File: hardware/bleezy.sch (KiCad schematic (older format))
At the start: 23 parts, among them P3 Raspberry_Pi_+_Conn

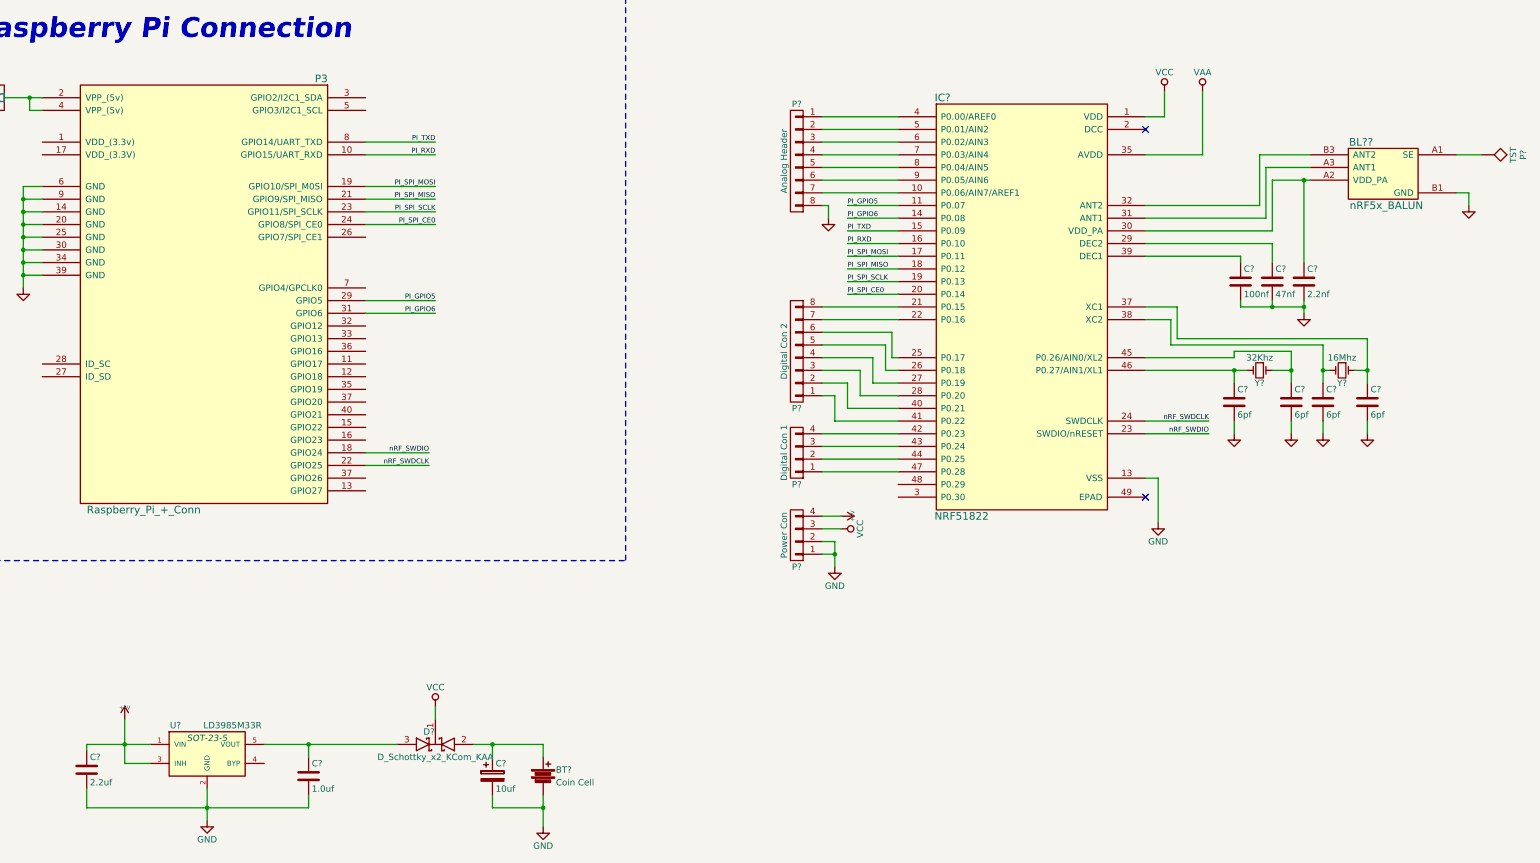
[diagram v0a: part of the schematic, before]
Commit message: added LED and vsense net
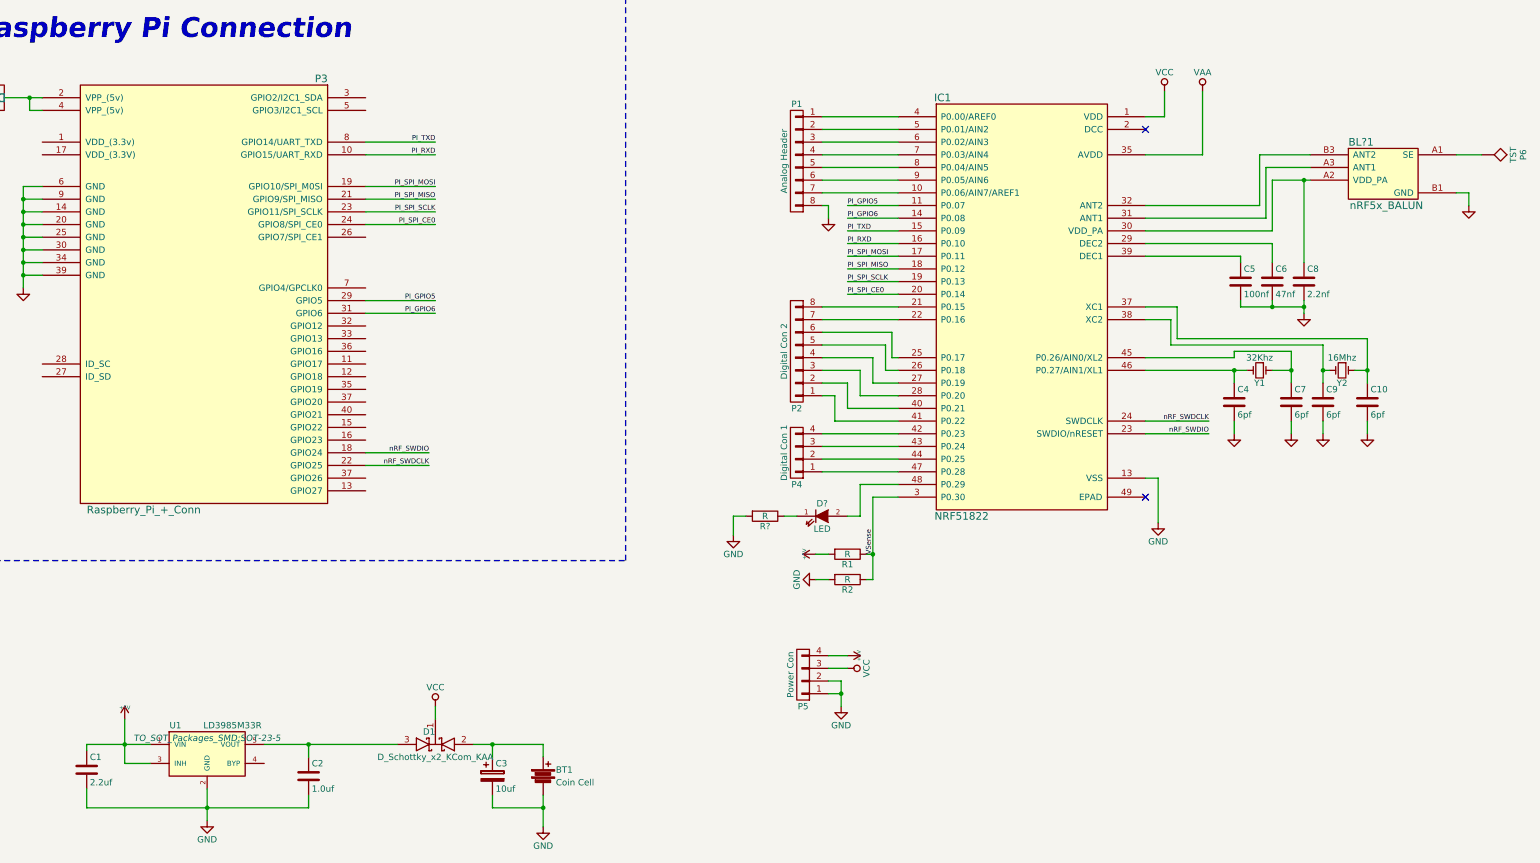
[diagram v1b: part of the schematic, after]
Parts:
- added D?: LED, symbol LED
- added R1, R2, R?: R, w_smd_resistors:r_0402, symbol R
- BL?1: renamed from BL??; footprint (none) -> openfet-footprint:BALUN_5BGA_ST
- BT1: renamed from BT?; footprint (none) -> openfet-footprint:keystone_3003
- C1, C10, C4, C5, C6, C7, C8, C9: renamed from C?; footprint (none) -> w_smd_cap:c_0402
- C2: renamed from C?; footprint (none) -> w_smd_cap:c_0603
- C3: renamed from C?; footprint (none) -> w_smd_cap:c_tant_B
- D1: renamed from D?; footprint (none) -> w_smd_trans:sot23
- IC1: renamed from IC?; footprint (none) -> w_smd_qfn:pvqfn-n48
- P1, P2: renamed from P?; footprint (none) -> w_pin_strip:pin_strip_8
- P4, P5: renamed from P?; footprint (none) -> w_pin_strip:pin_strip_4
- P6: renamed from P?; footprint (none) -> openfet-footprint:Ant_24ghz_small
- U1: renamed from U?; footprint SOT-23-5 -> TO_SOT_Packages_SMD:SOT-23-5
- Y1: renamed from Y?; footprint (none) -> w_crystal:crystal_tc-38_horiz
- Y2: renamed from Y?; footprint (none) -> w_crystal:crystal_fa128
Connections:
- net +5V: now also R1.2
- net GND: now also R2.2, R?.2
- net VSense: now reaches IC1.3 (P0.30)
- net VSense: now also R1.1, R2.1
- net at IC1.48 (P0.29): now also D?.2 (A)
- new net: D?.1 (K), R?.1
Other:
- moved on the sheet: P5

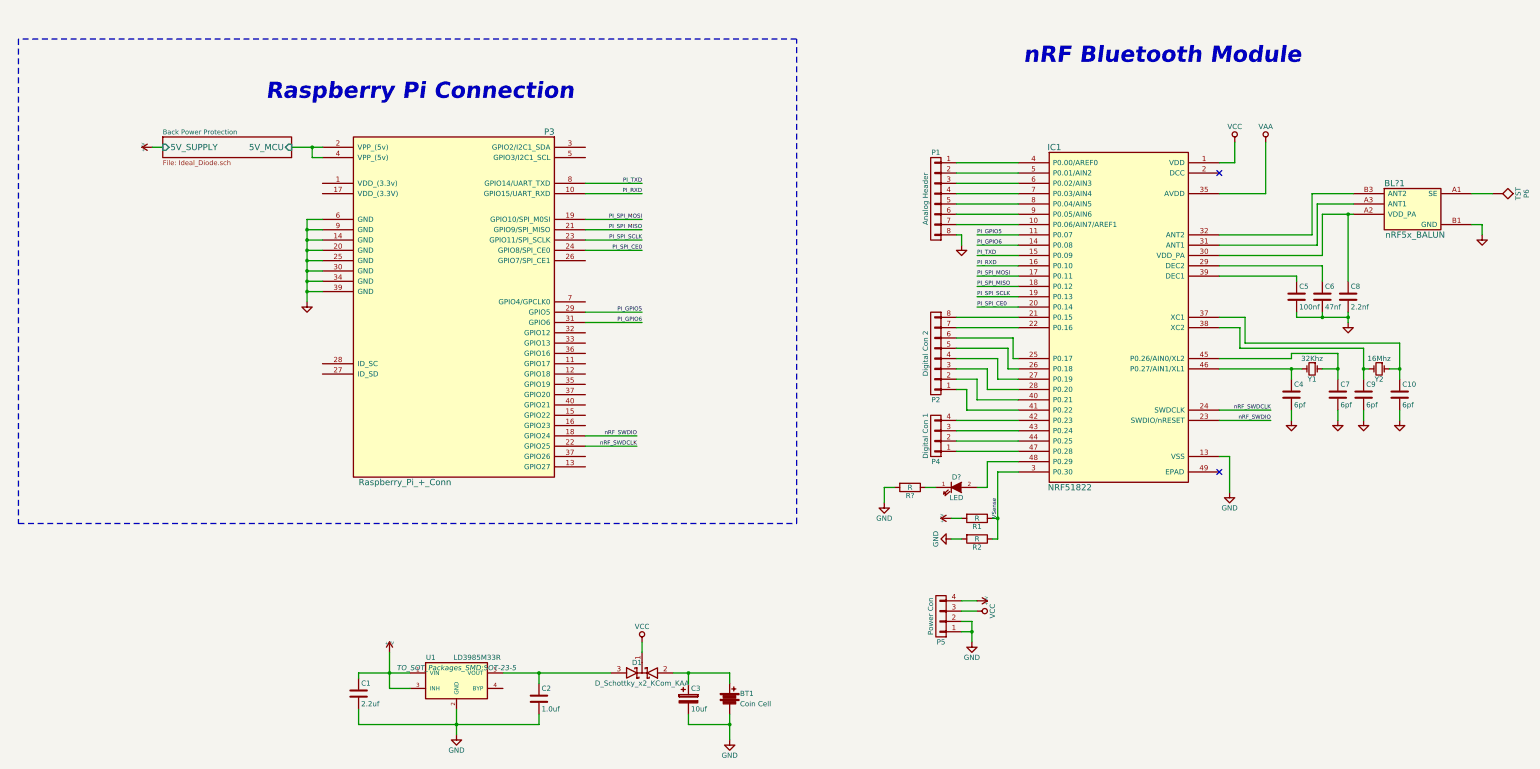
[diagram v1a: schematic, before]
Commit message: cleaned up schematic
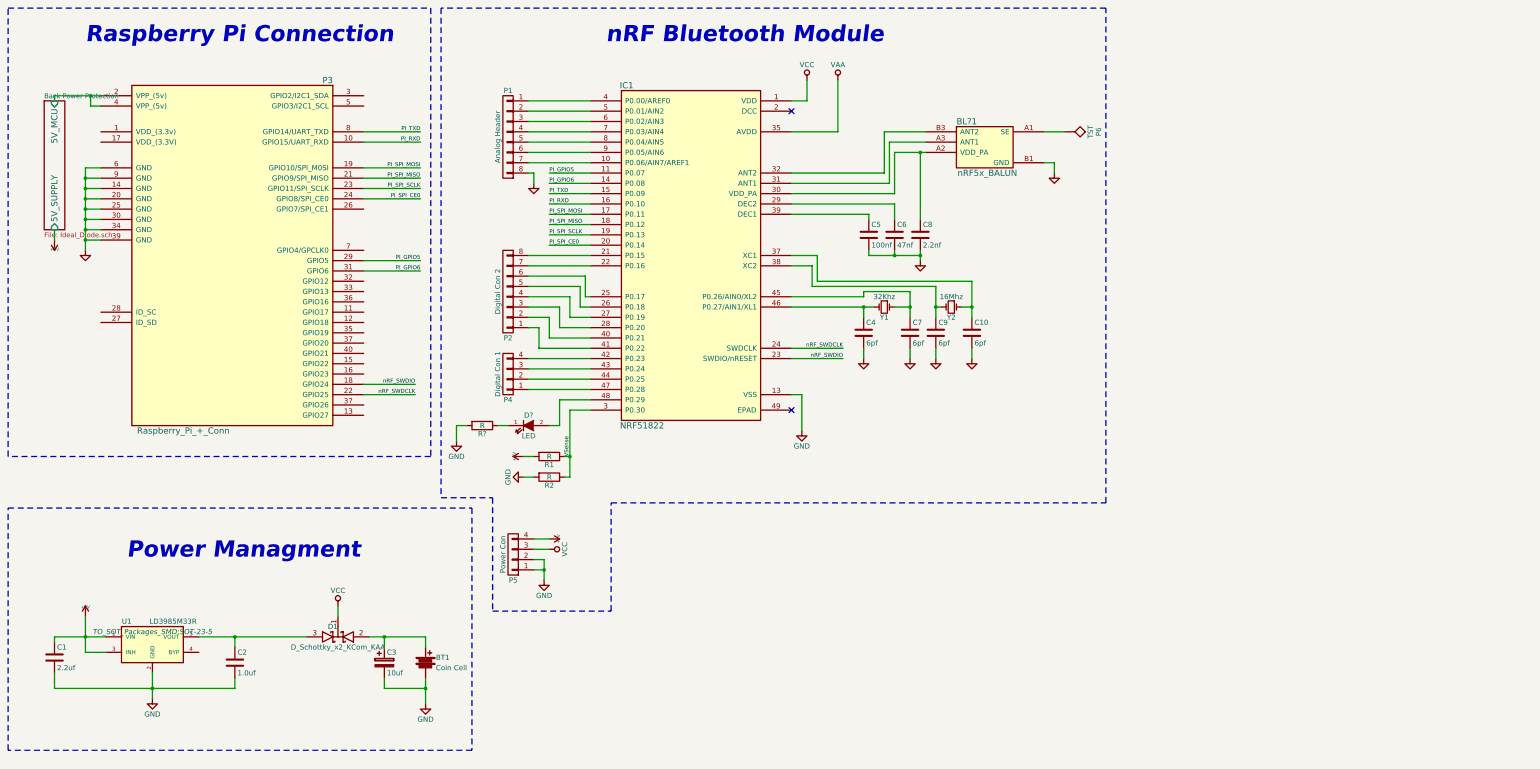
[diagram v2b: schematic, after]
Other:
- note added: "Power Managment"
- moved on the sheet: BL?1, BT1, C1, C10, C2, C3, C4, C5, C6, C7, C8, C9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

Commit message: removed monolithic balun
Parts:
- removed BL?1: nRF5x_BALUN, openfet-footprint:BALUN_5BGA_ST, symbol nRF5x_BALUN
- added C11: 2.2pf, w_smd_cap:c_0402, symbol C
- added C12: 1pf, w_smd_cap:c_0402, symbol C
- added C13: 1.5pf, w_smd_cap:c_0402, symbol C
- added JP1: JUMPER, w_smd_cap:c_0603, symbol JUMPER
- added L1: 4.7nH, w_smd_inductors:inductor_smd_0402, symbol INDUCTOR_SMALL
- added L2: 10nH, w_smd_inductors:inductor_smd_0402, symbol INDUCTOR_SMALL
- added L3: 3.3nH, w_smd_inductors:inductor_smd_0402, symbol INDUCTOR_SMALL
- D2: renamed from D?; footprint (none) -> w_smd_leds:Led_0603
- gave numbers to parts that had none: 1
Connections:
- net AVDD: now also JP1.2
- net GND: now also C12.1, C13.1
- net VCC: now also JP1.1
- net at C8.1, IC1.30 (VDD_PA): now also L2.1
- net at IC1.31 (ANT1): now also L1.1, L2.2
- net at IC1.32 (ANT2): now also C11.2, L1.2
- net at P6.1: now also C13.2, L3.1
- new net: C11.1, C12.2, L3.2
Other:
- moved on the sheet: P6

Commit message: redid basic layout, some routing
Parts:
- added C14, C15: 100nf, w_smd_cap:c_0402, symbol C
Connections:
- net GND: now also C14.2, C15.2
- net VCC: now also C14.1, C15.1
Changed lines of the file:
@@
 	0    -1   -1   0
 $EndComp
+$Comp
+L VCC #PWR027
+U 1 1 56861718
+P 10000 4450
+F 0 "#PWR027" H 10000 4300 50  0001 C CNN
+F 1 "VCC" H 10000 4600 50  0000 C CNN
+F 2 "" H 10000 4450 50  0000 C CNN
+F 3 "" H 10000 4450 50  0000 C CNN
+	1    10000 4450
+	1    0    0    -1
+$EndComp
+$Comp
+L C C14
+U 1 1 56861E04
+P 10000 4700
+F 0 "C14" H 10025 4800 50  0000 L CNN
+F 1 "100nf" H 10025 4600 50  0000 L CNN
+F 2 "w_smd_cap:c_0402" H 10038 4550 50  0001 C CNN
+F 3 "" H 10000 4700 50  0000 C CNN
+	1    10000 4700
+	1    0    0    -1
+$EndComp
+$Comp
+L GND #PWR028
+U 1 1 568620B4
+P 10000 4950
+F 0 "#PWR028" H 10000 4950 30  0001 C CNN
+F 1 "GND" H 10000 4880 30  0001 C CNN
+F 2 "" H 10000 4950 60  0000 C CNN
+F 3 "" H 10000 4950 60  0000 C CNN
+	1    10000 4950
+	1    0    0    -1
+$EndComp
+Wire Wire Line
+	10000 4550 10000 4450
+Wire Wire Line
+	10000 4850 10000 4950
+$Comp
+L C C15
+U 1 1 56862304
+P 10400 4700
+F 0 "C15" H 10425 4800 50  0000 L CNN
+F 1 "100nf" H 10425 4600 50  0000 L CNN
+F 2 "w_smd_cap:c_0402" H 10438 4550 50  0001 C CNN
+F 3 "" H 10400 4700 50  0000 C CNN
+	1    10400 4700
+	1    0    0    -1
+$EndComp
+Wire Wire Line
+	10000 4500 10400 4500
+Wire Wire Line
+	10400 4500 10400 4550
+Connection ~ 10000 4500
+Wire Wire Line
+	10000 4900 10400 4900
+Wire Wire Line
+	10400 4900 10400 4850
+Connection ~ 10000 4900
 $EndSCHEMATC

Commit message: finished routing
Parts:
- removed P4: Digital Con 1, w_pin_strip:pin_strip_4, symbol CONN_01X04
- D1: Mouser Part No. (none) -> 726-BAS7005E6327XT
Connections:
- net GND: now also IC1.49 (EPAD)
- no-connect marks 2 -> 1
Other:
- note added: "Note: This device is designed without any type of warrenty or garuntee. This\ndevice has no radio conformance cerification for any country."
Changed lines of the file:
@@
 LIBS:Zilog
 LIBS:nrf51822
+LIBS:xilinx7
+LIBS:xilinx6v
+LIBS:xilinx6s
+LIBS:xess
+LIBS:Lattice_iCE_FPGA
+LIBS:Cypress_PSoC
+LIBS:Cypress_cy8c5xlp
 LIBS:bleezy-cache
 EELAYER 25 0
@@
 encoding utf-8
 Sheet 1 2
-Title ""
-Date ""
-Rev ""
-Comp ""
-Comment1 ""
+Title "BLEezy"
+Date "2016-01-06"
+Rev "V0.1"
+Comp "OpenFET"
+Comment1 "Author: Julien M."
 Comment2 ""
 Comment3 ""
@@
 	1    0    0    -1
 $EndComp
-NoConn ~ 8100 4450
 $Comp
 L Crystal_Small Y2
@@
 $EndComp
 $Comp
-L CONN_01X04 P4
-U 1 1 5684B28F
-P 5350 4100
-F 0 "P4" H 5350 4350 50  0000 C CNN
-F 1 "Digital Con 1" V 5450 4100 50  0000 C CNN
-F 2 "w_pin_strip:pin_strip_4" H 5350 4100 50  0001 C CNN
-F 3 "" H 5350 4100 50  0000 C CNN
-	1    5350 4100
-	-1   0    0    1
-$EndComp
-$Comp
 L CONN_01X04 P5
 U 1 1 5684BC9A
@@
 F 0 "U1" H 1650 6900 50  0000 C CNN
 F 1 "LD3985M33R" H 2100 6900 50  0000 C CNN
-F 2 "TO_SOT_Packages_SMD:SOT-23-5" H 1900 6800 50  0000 C CIN
+F 2 "TO_SOT_Packages_SMD:SOT-23-5" H 1900 6800 50  0001 C CIN
 F 3 "" H 1900 6700 50  0000 C CNN
 	1    1900 6700
@@
 F 2 "w_smd_trans:sot23" H 3700 6650 50  0001 C CNN
 F 3 "" H 3700 6650 50  0000 C CNN
+F 4 "726-BAS7005E6327XT" H 3700 6650 60  0001 C CNN "Mouser Part No."
 	1    3700 6650
 	-1   0    0    1
@@
 	5650 3650 5550 3650
 Wire Wire Line
-	5550 3950 6150 3950
-Wire Wire Line
-	5550 4050 6150 4050
-Wire Wire Line
-	5550 4150 6150 4150
-Wire Wire Line
-	5550 4250 6150 4250
-Wire Wire Line
 	5600 6000 5700 6000
 Wire Wire Line
@@
 	10400 4900 10400 4850
 Connection ~ 10000 4900
+Wire Wire Line
+	8100 4450 8200 4450
+Connection ~ 8200 4450
+Text Notes 6950 6400 0    60   ~ 0
+Note: This device is designed without any type of warrenty or garuntee. This\ndevice has no radio conformance cerification for any country.
 $EndSCHEMATC

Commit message: added some to do
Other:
- note added: "To Do:\n- setup the traces for better PCB routing\n- add gaurd ring to the crystal\n- add the DC/DC to the nRF module\n- make sheet bigger"
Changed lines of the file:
@@
 Text Notes 6950 6400 0    60   ~ 0
 Note: This device is designed without any type of warrenty or garuntee. This\ndevice has no radio conformance cerification for any country.
+Text Notes 6950 6000 0    60   ~ 0
+To Do:\n- setup the traces for better PCB routing\n- add gaurd ring to the crystal\n- add the DC/DC to the nRF module\n- make sheet bigger
 $EndSCHEMATC

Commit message: added DC/DC, changed some pinouts
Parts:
- added C16: 1.0uf, w_smd_cap:c_0402, symbol C
- added L5: 10uH, w_smd_inductors:inductor_smd_0603, symbol INDUCTOR_SMALL
- added L6: 15nH, w_smd_inductors:inductor_smd_0402, symbol INDUCTOR_SMALL
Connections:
- net AVDD: now also C16.2, L6.1
- net GND: now also C16.1
- net PI_GPIO5: now also IC1.20 (P0.14); no longer IC1.11 (P0.07)
- net PI_GPIO6: now also IC1.19 (P0.13); no longer IC1.14 (P0.08)
- net PI_RXD: now also IC1.27 (P0.19); no longer IC1.16 (P0.10)
- net PI_SPI_CE0: now also IC1.21 (P0.15); no longer IC1.20 (P0.14)
- net PI_SPI_MISO: now also IC1.25 (P0.17); no longer IC1.18 (P0.12)
- net PI_SPI_MOSI: now also IC1.26 (P0.18); no longer IC1.17 (P0.11)
- net PI_SPI_SCLK: now also IC1.22 (P0.16); no longer IC1.19 (P0.13)
- net PI_TXD: now also IC1.28 (P0.20); no longer IC1.15 (P0.09)
- net P0.06: now reaches IC1.10 (P0.06/AIN7/AREF1), P1.7 (P7)
- net at IC1.2 (DCC): now also L5.2
- net P0.21: now reaches P2.8 (P8)
- net P0.21: now also IC1.40 (P0.21); no longer IC1.21 (P0.15)
- net P0.22: now reaches P2.7 (P7)
- net P0.22: now also IC1.41 (P0.22); no longer IC1.22 (P0.16)
- net P0.23: now reaches P2.6 (P6)
- net P0.23: now also IC1.42 (P0.23); no longer IC1.25 (P0.17)
- net P0.24: now reaches P2.5 (P5)
- net P0.24: now also IC1.43 (P0.24); no longer IC1.26 (P0.18)
- net P0.25: now reaches P2.4 (P4)
- net P0.25: now also IC1.44 (P0.25); no longer IC1.27 (P0.19)
- net P0.12: now reaches P2.3 (P3)
- net P0.12: now also IC1.16 (P0.10); no longer IC1.28 (P0.20)
- net P0.00: now reaches IC1.4 (P0.00/AREF0), P1.1 (P1)
- net P0.11: now reaches P2.2 (P2)
- net P0.11: now also IC1.17 (P0.11); no longer IC1.40 (P0.21)
- net P0.13: now reaches P2.1 (P1)
- net P0.13: now also IC1.18 (P0.12); no longer IC1.41 (P0.22)
- net P0.01: now reaches IC1.5 (P0.01/AIN2), P1.2 (P2)
- net P0.02: now reaches IC1.6 (P0.02/AIN3), P1.3 (P3)
- net P0.03: now reaches IC1.7 (P0.03/AIN4), P1.4 (P4)
- net P0.04: now reaches IC1.8 (P0.04/AIN5), P1.5 (P5)
- net P0.05: now reaches IC1.9 (P0.05/AIN6), P1.6 (P6)
- new net: L5.1, L6.2
- no-connect marks 1 -> 0
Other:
- moved on the sheet: BT1, C1, C10, C11, C12, C13, C14, C15, C2, C3, C4, C5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
